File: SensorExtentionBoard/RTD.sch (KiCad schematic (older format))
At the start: 100 parts

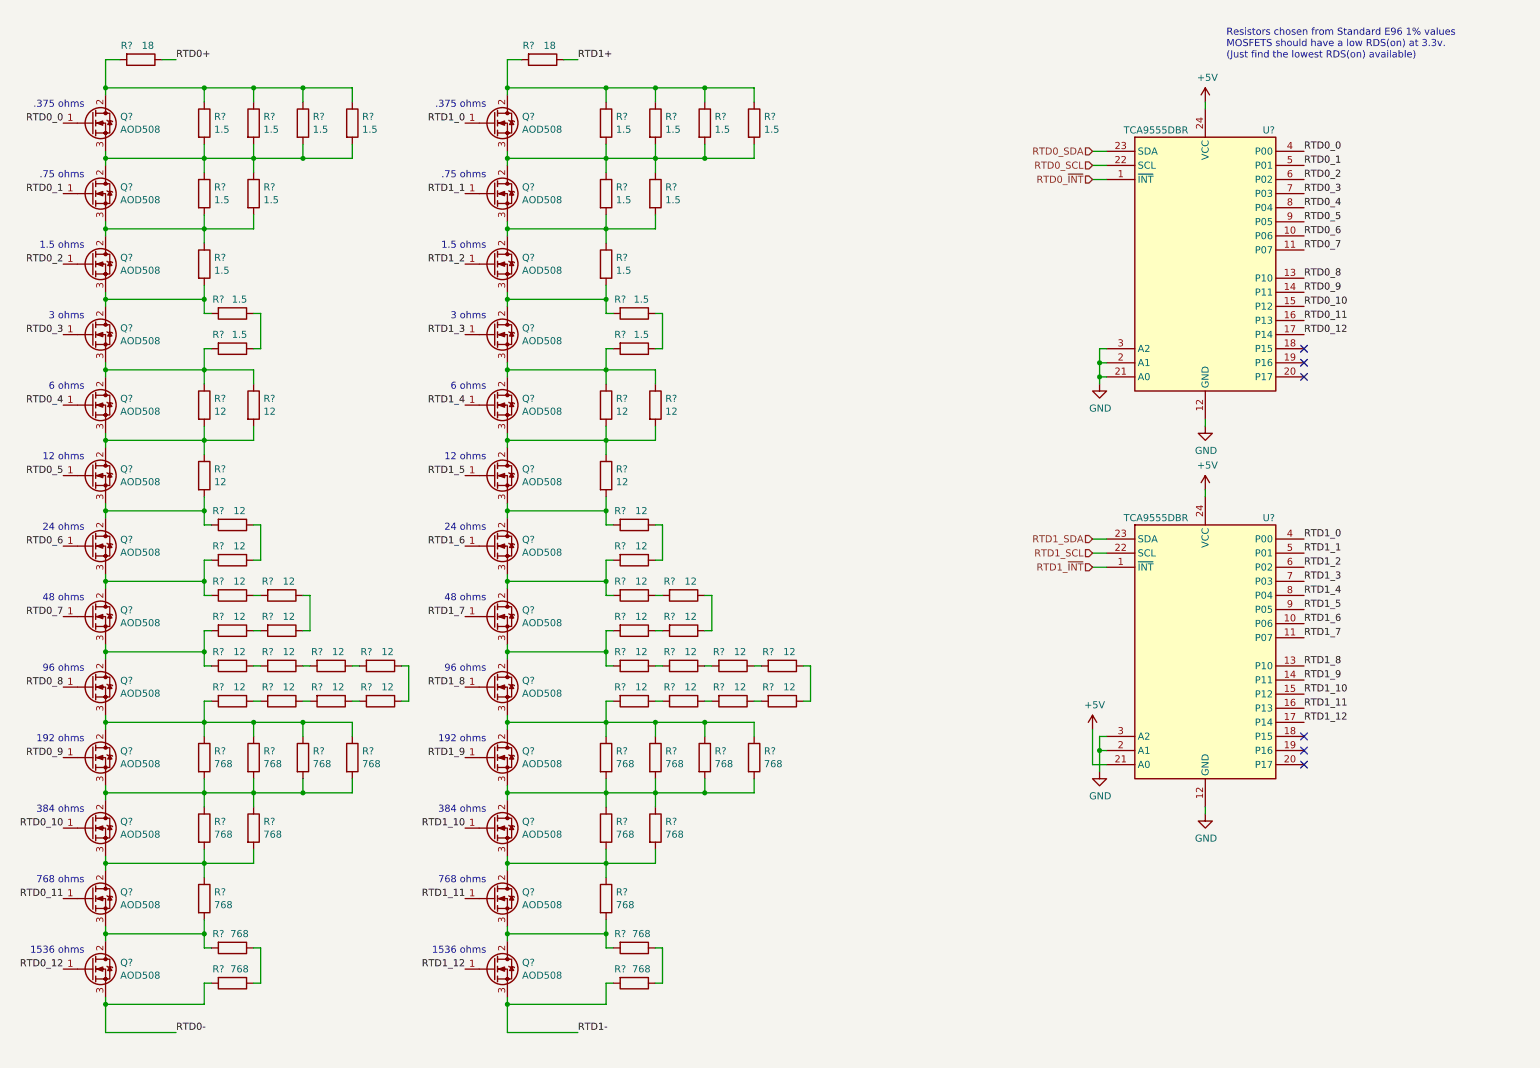
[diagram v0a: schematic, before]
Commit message: Added short circuit and open circuit test functionality to RTD test circuit
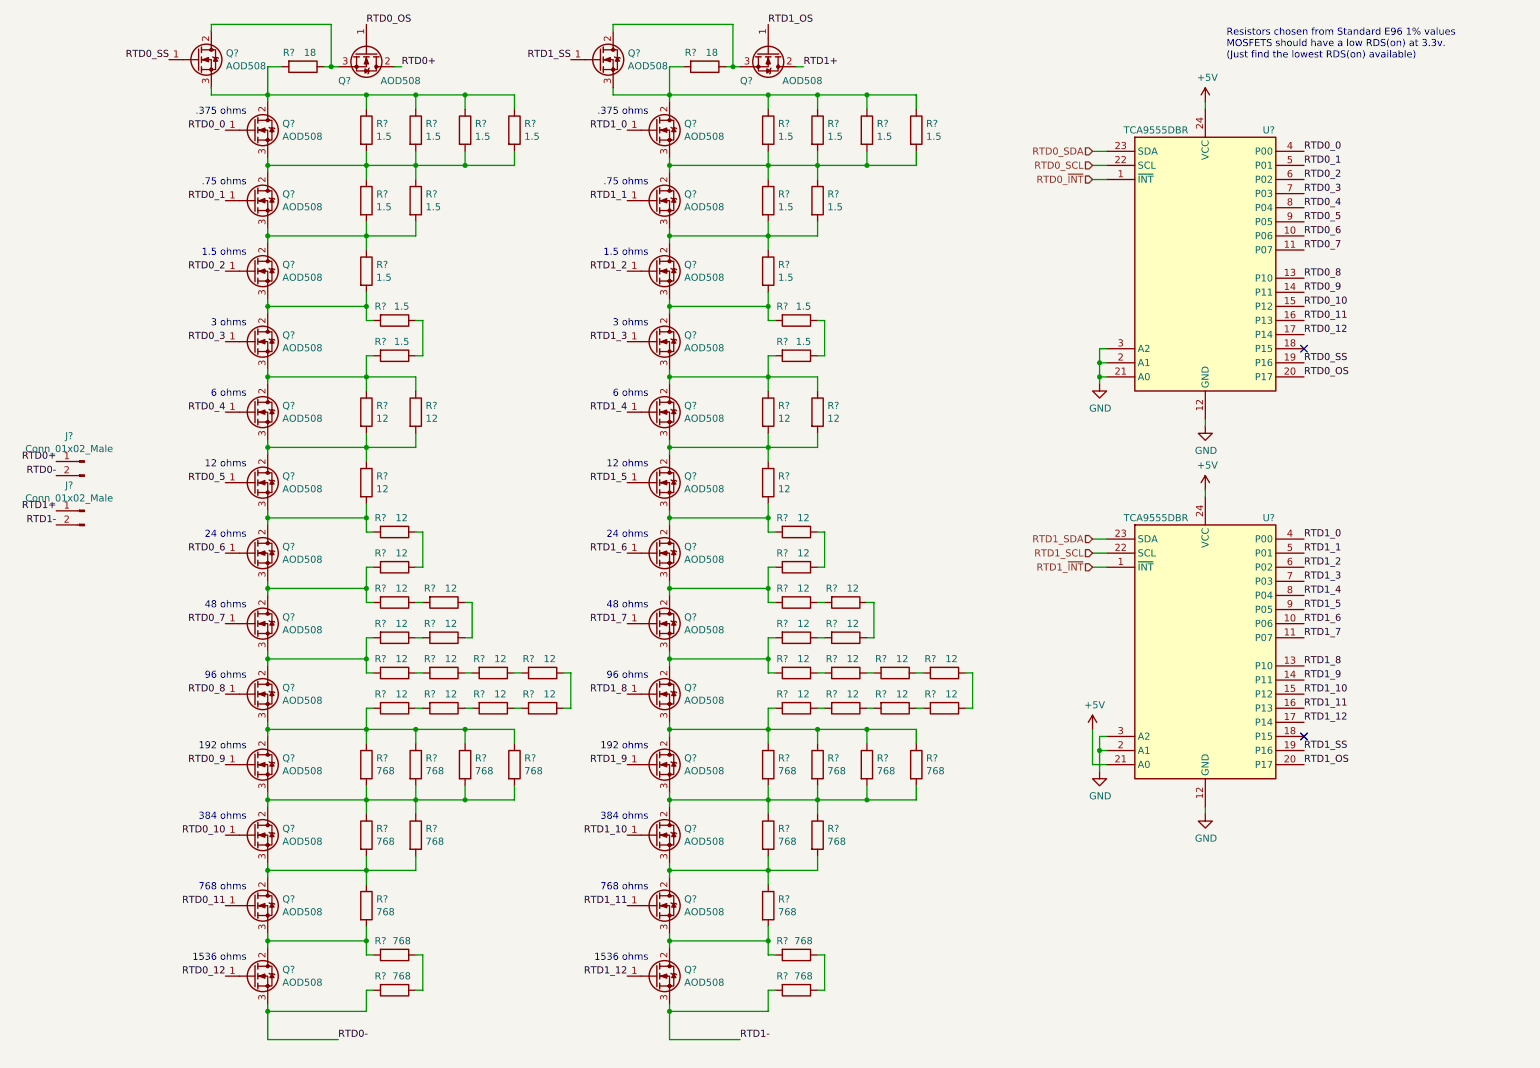
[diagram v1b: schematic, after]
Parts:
- removed R?: 18, symbol Device:R
- added J? (x2): Conn_01x02_Male, Connector_Molex:Molex_Micro-Fit_3.0_43650-0215_1x02_P3.00mm_Vertical, symbol Connector:Conn_01x02_Male
- added Q? (x4): AOD508, Package_TO_SOT_SMD:TO-252-3_TabPin2, symbol Device:Q_NMOS_GDS
- added R?: 18, symbol Device:R
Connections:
- net RTD0+: now also J?.1 (Pin_1), Q?.2 (D)
- net RTD0-: now also J?.2 (Pin_2)
- net RTD1+: now also J?.1 (Pin_1), Q?.2 (D); no longer R?.1
- net RTD1-: now also J?.2 (Pin_2)
- net at Q?.2 (D), R?.1, R?.1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: now also Q?.3 (S)
- net at Q?.2 (D), R?.1, R?.1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: now also Q?.3 (S), R?.2
- net RTD0_SS: now reaches U?.19 (P16)
- net RTD0_SS: now also Q?.1 (G)
- net RTD0_OS: now reaches U?.20 (P17)
- net RTD0_OS: now also Q?.1 (G)
- net RTD1_SS: now reaches U?.19 (P16)
- net RTD1_SS: now also Q?.1 (G)
- net RTD1_OS: now reaches U?.20 (P17)
- net RTD1_OS: now also Q?.1 (G)
- new net: Q?.2 (D), Q?.3 (S), R?.1 (x2)
- no-connect marks 6 -> 2
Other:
- moved on the sheet: Q?, R?

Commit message: Added top level page and made various fixes in other pages of SEB test rig board
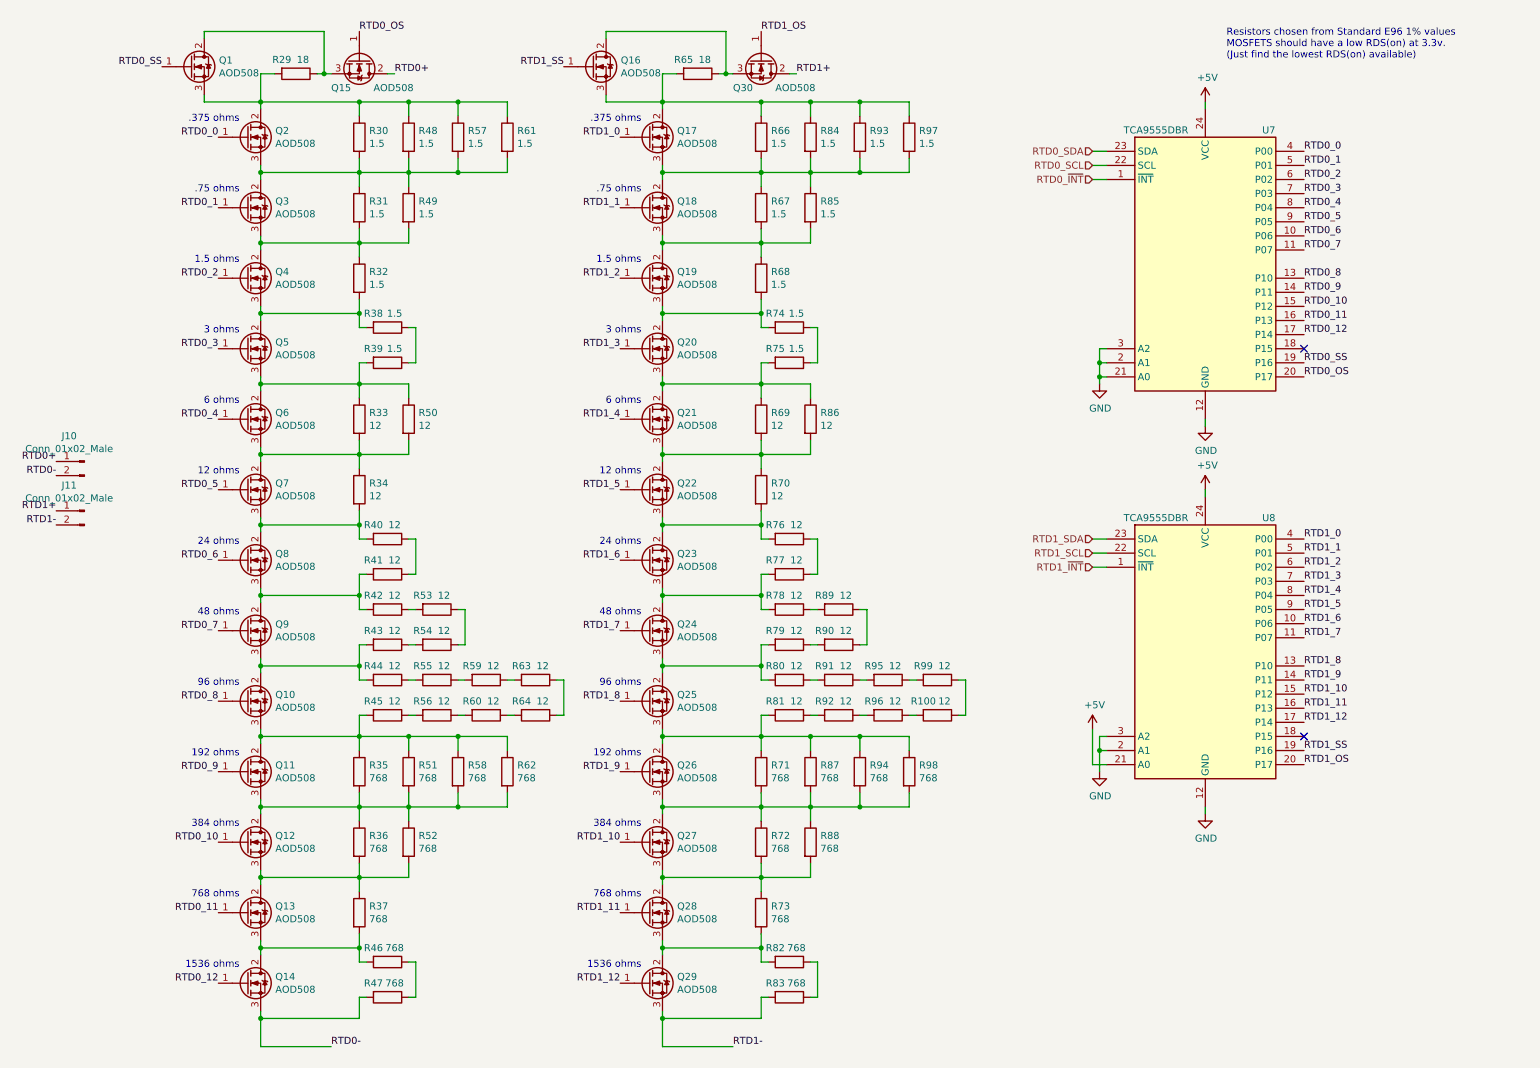
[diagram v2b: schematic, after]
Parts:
- R100, R29, R30, R31, R32, R33, R34, R35, R36, R37, R38, R39, R40, R41, R42, R43, R44, R45, R46, R47, R48, R49, R50, R51, R52, R53, R54, R55, R56, R57, R58, R59, R60, R61, R62, R63, R64, R65, R66, R67, R68, R69, R70, R71, R72, R73, R74, R75, R76, R77, R78, R79, R80, R81, R82, R83, R84, R85, R86, R87, R88, R89, R90, R91, R92, R93, R94, R95, R96, R97, R98, R99: renamed from R?; footprint (none) -> Resistor_SMD:R_1206_3216Metric_Pad1.42x1.75mm_HandSolder
- gave numbers to parts that had none: 34
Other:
- moved on the sheet: Q1, Q10, Q11, Q12, Q13, Q14, Q15, Q16, Q17, Q18, Q19, Q2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

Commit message: Moved some stuff and added footprints to components
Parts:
- J10, J11: footprint Connector_Molex:Molex_Micro-Fit_3.0_43650-0215_1x02_P3.00mm_Vertical -> Connector_Molex:Molex_MicroClasp_55932-0210_1x02_P2.00mm_Vertical
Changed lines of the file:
@@
 F 0 "J10" H 1158 3781 50  0000 C CNN
 F 1 "Conn_01x02_Male" H 1158 3690 50  0000 C CNN
-F 2 "Connector_Molex:Molex_Micro-Fit_3.0_43650-0215_1x02_P3.00mm_Vertical" H 1050 3600 50  0001 C CNN
+F 2 "Connector_Molex:Molex_MicroClasp_55932-0210_1x02_P2.00mm_Vertical" H 1050 3600 50  0001 C CNN
 F 3 "~" H 1050 3600 50  0001 C CNN
 	1    1050 3600
@@
 F 0 "J11" H 1158 4131 50  0000 C CNN
 F 1 "Conn_01x02_Male" H 1158 4040 50  0000 C CNN
-F 2 "Connector_Molex:Molex_Micro-Fit_3.0_43650-0215_1x02_P3.00mm_Vertical" H 1050 3950 50  0001 C CNN
+F 2 "Connector_Molex:Molex_MicroClasp_55932-0210_1x02_P2.00mm_Vertical" H 1050 3950 50  0001 C CNN
 F 3 "~" H 1050 3950 50  0001 C CNN
 	1    1050 3950

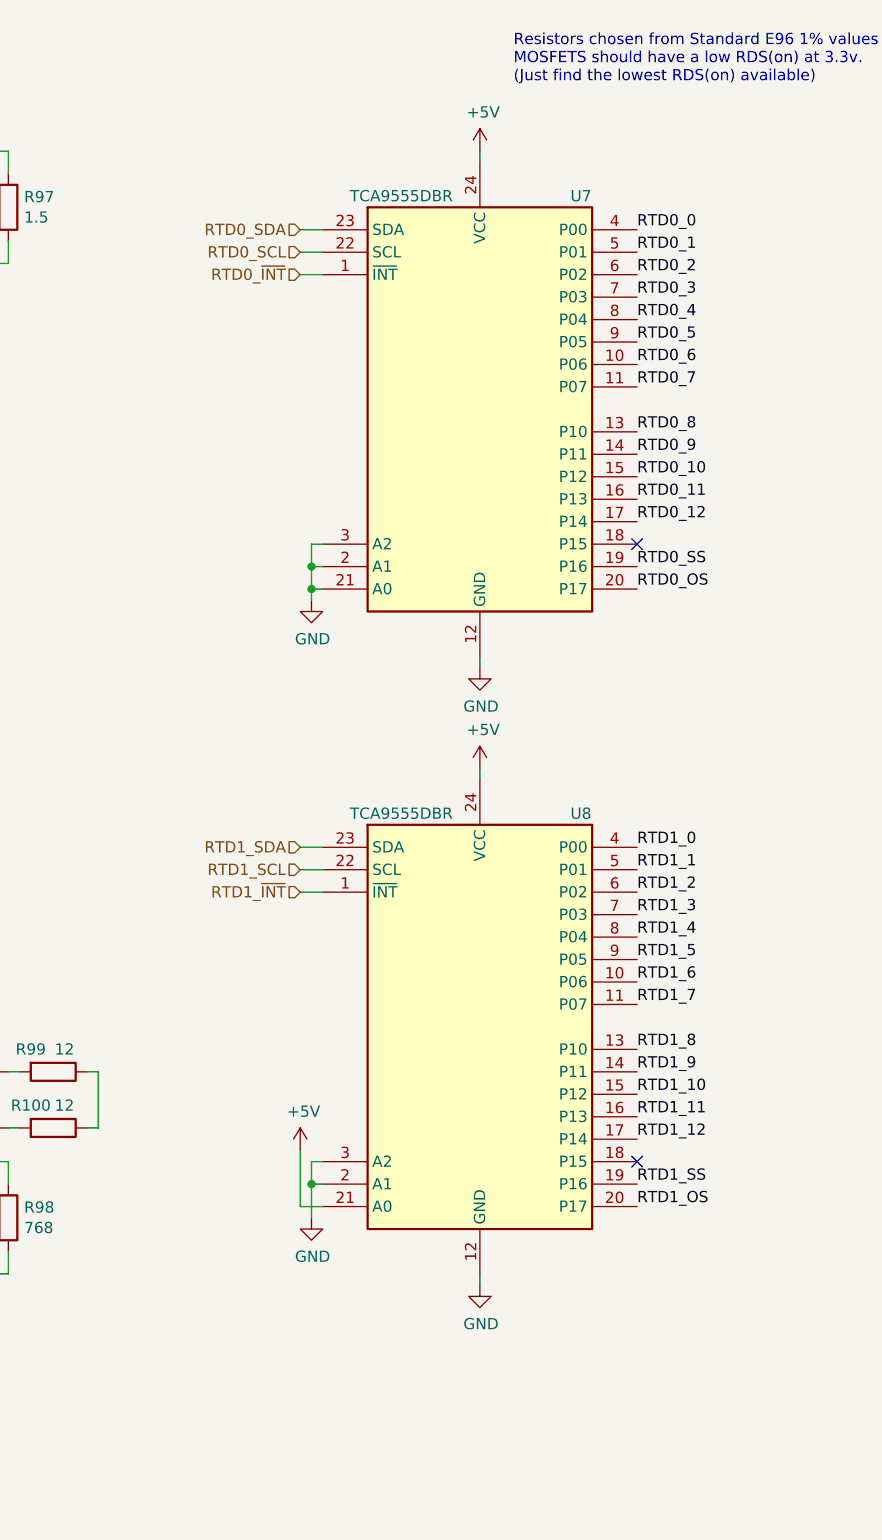
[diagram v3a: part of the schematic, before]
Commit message: Added decoupling caps
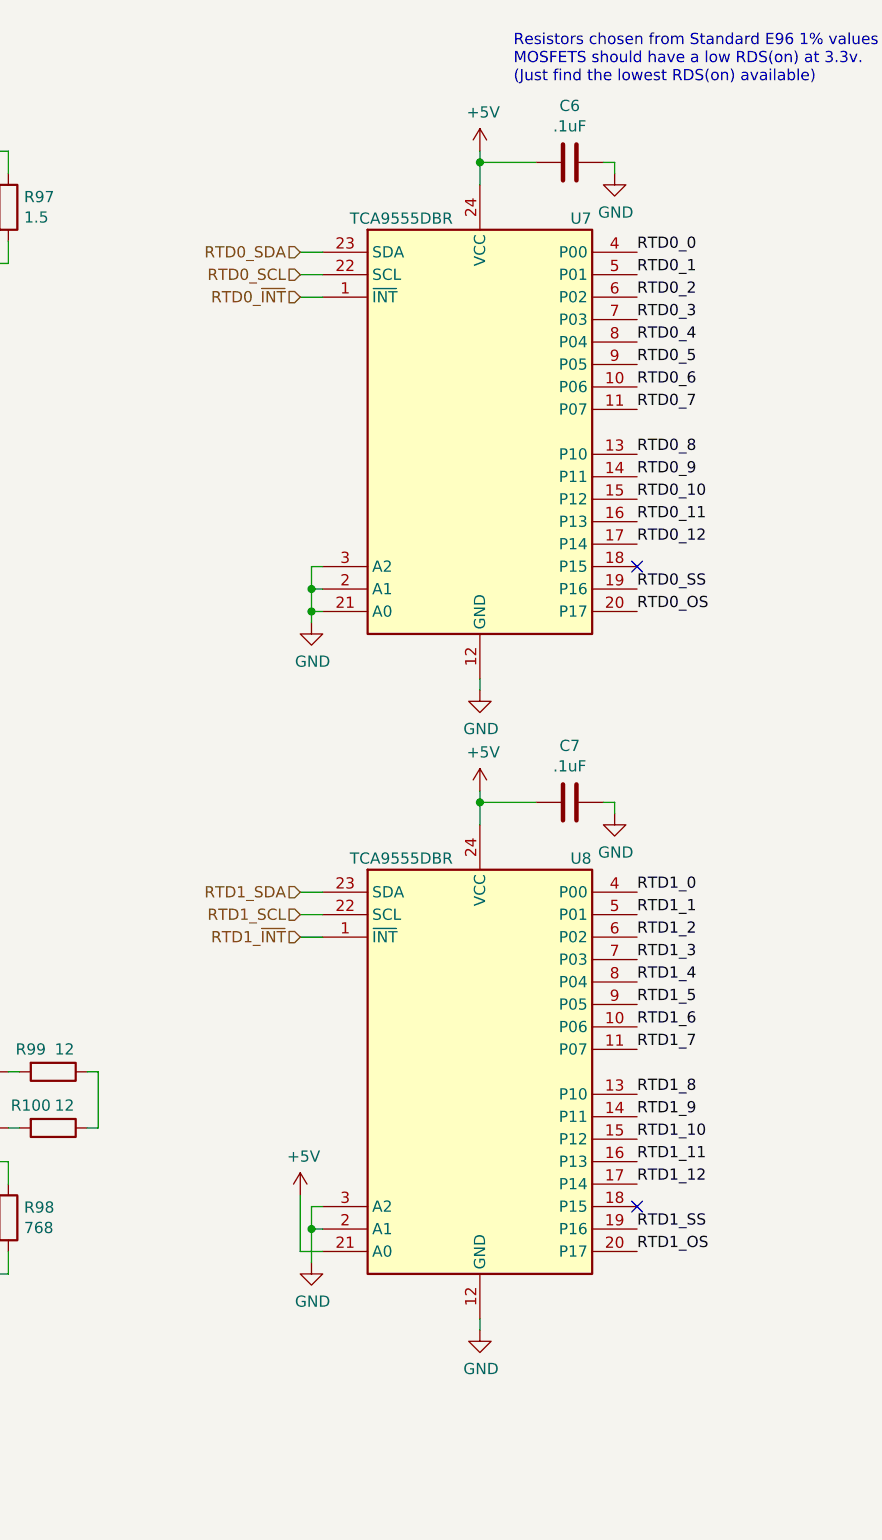
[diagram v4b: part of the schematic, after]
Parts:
- added C6, C7: .1uF, symbol Device:C
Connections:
- net +5V: now also C6.2, C7.2
- net GND: now also C6.1, C7.1
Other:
- moved on the sheet: U7, U8

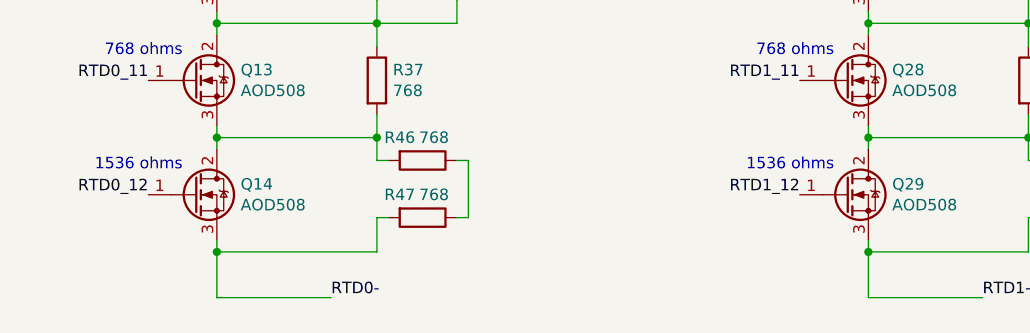
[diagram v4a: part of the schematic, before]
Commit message: Added ground reference for RTD test section
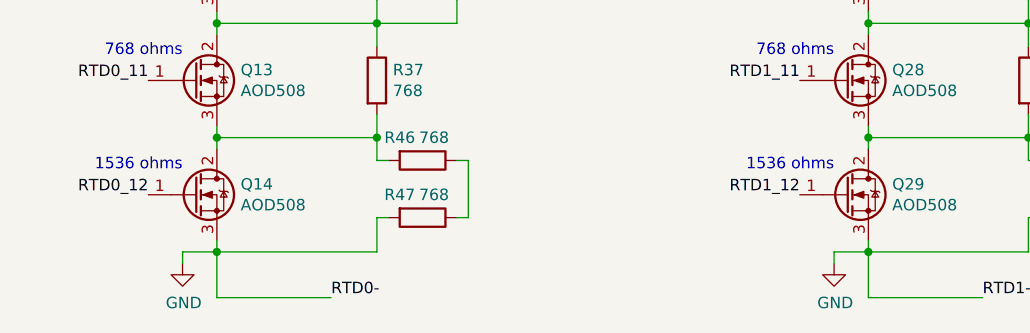
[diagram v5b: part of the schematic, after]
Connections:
- net RTD0- is gone; now on net GND: J10.2 (Pin_2), Q14.3 (S), R47.2
- net RTD1- is gone; now on net GND: J11.2 (Pin_2), Q29.3 (S), R83.2
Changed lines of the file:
@@
 Wire Wire Line
 	9000 3950 9000 4050
+$Comp
+L power:GND #PWR?
+U 1 1 5E1B7251
+P 2150 7600
+F 0 "#PWR?" H 2150 7350 50  0001 C CNN
+F 1 "GND" H 2155 7427 50  0000 C CNN
+F 2 "" H 2150 7600 50  0001 C CNN
+F 3 "" H 2150 7600 50  0001 C CNN
+	1    2150 7600
+	1    0    0    -1
+$EndComp
+Wire Wire Line
+	2150 7600 2150 7550
+Wire Wire Line
+	2150 7550 2300 7550
+$Comp
+L power:GND #PWR?
+U 1 1 5E1D1E5B
+P 5000 7600
+F 0 "#PWR?" H 5000 7350 50  0001 C CNN
+F 1 "GND" H 5005 7427 50  0000 C CNN
+F 2 "" H 5000 7600 50  0001 C CNN
+F 3 "" H 5000 7600 50  0001 C CNN
+	1    5000 7600
+	1    0    0    -1
+$EndComp
+Wire Wire Line
+	5000 7600 5000 7550
+Wire Wire Line
+	5000 7550 5150 7550
 $EndSCHEMATC
